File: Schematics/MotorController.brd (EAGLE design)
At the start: 90 x 80 mm, 47 parts, among them IC1 MEGA164P/324P/644P-AU, IC3 LM324N

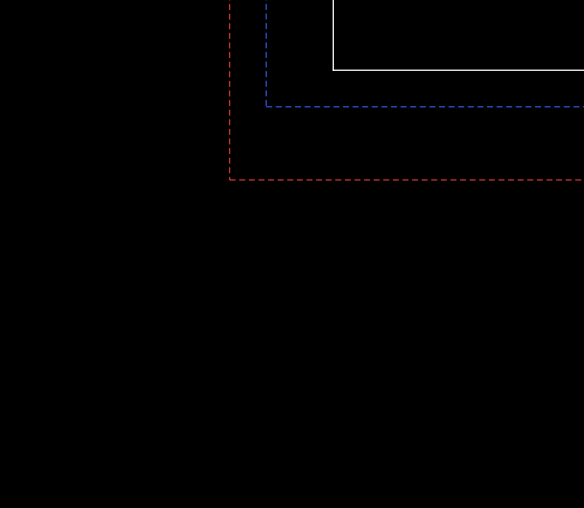
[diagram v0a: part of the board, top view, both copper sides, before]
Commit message: add files of device software newly created
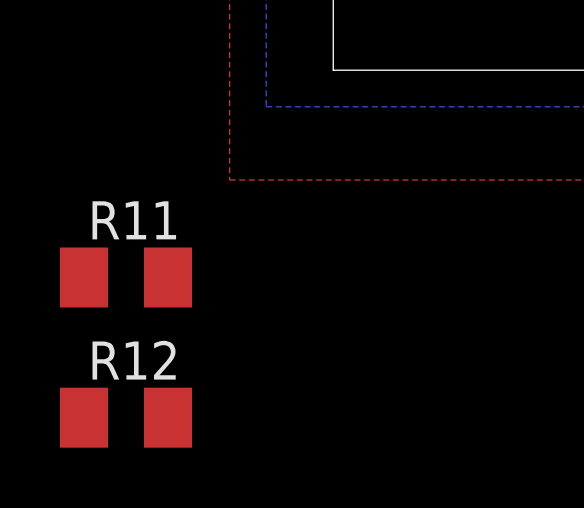
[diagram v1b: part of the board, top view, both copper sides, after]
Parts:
- added R11, R12: (no value), rcl:M3216
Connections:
- new net N$14: R10.2, R11.1, R12.1
- net +5V: no longer C11.2
- net A_BACK: now also R11.2; no longer R10.2
- net GND: now also C11.2, R12.2
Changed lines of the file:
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@@
 <element name="C14" library="rcl" package="C3216" value="" x="15.664" y="30.1504"/>
 <element name="L2" library="rcl" package="L3216C" value="" x="36" y="22" rot="R180"/>
+<element name="R11" library="rcl" package="M3216" value="" x="-6.9088" y="-6.9088"/>
+<element name="R12" library="rcl" package="M3216" value="" x="-6.9088" y="-11.5824"/>
 </elements>
 <signals>
@@
 <contactref element="C6" pad="2"/>
 <contactref element="C7" pad="2"/>
-<contactref element="C8" pad="1"/>
-<contactref element="C11" pad="2"/>
 <contactref element="U$3" pad="3"/>
 <contactref element="L2" pad="1"/>
-<wire x1="9.74" y1="48.26" x2="25.28" y2="50.18" width="0" layer="19" extent="1-1"/>
-<wire x1="6.6664" y1="53.7" x2="9.74" y2="48.26" width="0" layer="19" extent="1-1"/>
-<wire x1="10.0728" y1="34.504" x2="9.74" y2="48.26" width="0" layer="19" extent="1-1"/>
-<wire x1="4.29" y1="34.53" x2="10.0728" y2="34.504" width="0" layer="19" extent="1-1"/>
+<contactref element="C8" pad="1"/>
+<wire x1="6.6664" y1="53.7" x2="25.28" y2="50.18" width="0" layer="19" extent="1-1"/>
+<wire x1="4.29" y1="34.53" x2="6.6664" y2="53.7" width="0" layer="19" extent="1-1"/>
+<wire x1="10.0728" y1="34.504" x2="4.29" y2="34.53" width="0" layer="19" extent="1-1"/>
 <wire x1="6.896" y1="22.7052" x2="4.29" y2="34.53" width="0" layer="19" extent="1-1"/>
 <wire x1="12.934" y1="16.93" x2="6.896" y2="22.7052" width="0" layer="19" extent="1-1"/>
@@
 <vertex x="94.2848" y="84.1248"/>
 </polygon>
+<contactref element="C11" pad="2"/>
+<contactref element="R12" pad="2"/>
 <wire x1="30.45" y1="63.58" x2="36.16" y2="75.42" width="0" layer="19" extent="1-1"/>
 <wire x1="26.976" y1="62.58" x2="30.45" y2="63.58" width="0" layer="19" extent="1-1"/>
@@
 <wire x1="15.28" y1="53.68" x2="15.28" y2="56.18" width="0" layer="19" extent="1-1"/>
 <wire x1="15.28" y1="51.18" x2="15.28" y2="53.68" width="0" layer="19" extent="1-1"/>
-<wire x1="9.1796" y1="55.9536" x2="15.28" y2="56.18" width="0" layer="19" extent="1-1"/>
+<wire x1="9.22" y1="51.3328" x2="15.28" y2="51.18" width="0" layer="19" extent="1-1"/>
+<wire x1="9.74" y1="48.26" x2="9.22" y2="51.3328" width="0" layer="19" extent="1-1"/>
+<wire x1="9.1796" y1="55.9536" x2="9.22" y2="51.3328" width="0" layer="19" extent="1-1"/>
 <wire x1="6.6664" y1="55.4" x2="9.1796" y2="55.9536" width="0" layer="19" extent="1-1"/>
 <wire x1="6.74" y1="57.66" x2="6.6664" y2="55.4" width="0" layer="19" extent="1-1"/>
-<wire x1="9.22" y1="51.3328" x2="6.6664" y2="55.4" width="0" layer="19" extent="1-1"/>
-<wire x1="6.83" y1="42.15" x2="9.22" y2="51.3328" width="0" layer="19" extent="1-1"/>
+<wire x1="6.83" y1="42.15" x2="9.74" y2="48.26" width="0" layer="19" extent="1-1"/>
 <wire x1="9.8896" y1="38.3424" x2="6.83" y2="42.15" width="0" layer="19" extent="1-1"/>
 <wire x1="6.83" y1="31.99" x2="9.8896" y2="38.3424" width="0" layer="19" extent="1-1"/>
@@
 <wire x1="25.8064" y1="40.9956" x2="25.28" y2="51.18" width="0" layer="19" extent="1-1"/>
 <wire x1="4" y1="71.2" x2="15.6" y2="64.08" width="0" layer="19" extent="1-1"/>
+<wire x1="-5.5088" y1="-11.5824" x2="13.25" y2="8.26" width="0" layer="19" extent="1-1"/>
 </signal>
 <signal name="MISO">
@@
 <contactref element="D6" pad="E"/>
 <contactref element="D7" pad="E"/>
-<contactref element="R10" pad="2"/>
+<contactref element="R11" pad="2"/>
 <wire x1="3.7628" y1="62.8" x2="7.3564" y2="62.8" width="0" layer="19" extent="1-1"/>
-<wire x1="10.4992" y1="27.3056" x2="7.3564" y2="62.8" width="0" layer="19" extent="1-1"/>
+<wire x1="-5.5088" y1="-6.9088" x2="3.7628" y2="62.8" width="0" layer="19" extent="1-1"/>
 </signal>
 <signal name="N$6">
@@
 <wire x1="31.89553125" y1="18.826903125" x2="34.5" y2="22" width="0" layer="19" extent="1-1"/>
 </signal>
+<signal name="N$14">
+<contactref element="R10" pad="2"/>
+<contactref element="R12" pad="1"/>
+<contactref element="R11" pad="1"/>
+<wire x1="-8.3088" y1="-6.9088" x2="10.4992" y2="27.3056" width="0" layer="19" extent="1-1"/>
+<wire x1="-8.3088" y1="-11.5824" x2="-8.3088" y2="-6.9088" width="0" layer="19" extent="1-1"/>
+</signal>
 </signals>

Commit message: restoring
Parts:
- removed D5, D6, D7, D8: 1SS196, myparts:SC59-BEC
- removed L2: (no value), rcl:L3216C
- removed U$5: TLP621-2, myparts:SOCKET-08
- removed U$6, U$7: XH-2, myparts:XH-2
- added A, B, C, D: 942H, myparts:941H-2C-12D
- added A_NEXT, A_PREV, B_NEXT, B_PREV, C_NEXT, C_PREV, D_NEXT, D_PREV: XH-2, myparts:XH-2
- added C15, C18, C19, C24, C25: 0.1u, rcl:C0603
- added C16, C17: 0.47u, rcl:C0603
- added C20, C21: 22p, rcl:C0603
- added C22, C23: 4.7u, rcl:C0603
- added C26, C27: (no value), rcl:E2,5-6E
- added CONN: TUS_MODULE_SUPPLY, tus:2X08
- added F1, F2, F3, F4, F5: POLYSWITCH_20204/5, myparts:0204/5
- added IC2: MEGA164P/324P/644P-AU, avr-7:TQFP44
- added IC4: TLP621-2, myparts:SOCKET-08
- added LED3, LED5, LED7: G, led:LED3MM
- added LED4, LED6, LED8: O, led:LED3MM
- added R13, R14, R23, R24: 100, resistor:R0603
- added R15, R16, R22, R25: 25k, resistor:R0603
- added R17, R18, R20, R21, R30, R31: 3.3k, resistor:R0603
- added R19, R36, R37: 10k, resistor:R0603
- added R26, R27: 0.01, resistor:R1206
- added R28, R29: 33k, resistor:R0603
- added R32, R33: 500, resistor:R0603
- added R34, R35: 100k, resistor:R0603
- added T1, T2, T3, T4: 2SC1815, myparts:TO92-ECB
- C1, C2: device rcl:C1608 -> rcl:E2,5-6E
- C10: value (none) -> 0.47u; device rcl:E2-5 -> rcl:C0603
- C11, C7, C8: value (none) -> 0.1u; device rcl:C1608 -> rcl:C0603
- C12: value (none) -> 100u; device rcl:C1608 -> rcl:E2,5-6
- C13: value (none) -> 0.1u; device rcl:C3216 -> rcl:C0603
- C14: value (none) -> 100u; device rcl:C3216 -> rcl:E2-5
- C3: value (none) -> 0.1u; device rcl:E2-5 -> rcl:C0603
- C4: value (none) -> 0.1u; device rcl:E2,5-6 -> rcl:C0603
- C5, C6: value (none) -> 4.7u; device rcl:C1608 -> rcl:C0603
- C9: value (none) -> 0.47u; device rcl:C1608 -> rcl:C0603
- D1, D2, D3, D4: value 1SS196 -> 1N4148DO35-7; device myparts:SC59-BEC -> diode:DO35-7
- IC1: value MEGA164P/324P/644P-AU -> TLP621-2; device avr-7:TQFP44 -> myparts:SOCKET-08
- IC3: value LM324N -> OPA4234P; device linear:DIL14 -> burr-brown:DIL14
- JP1: value AVR-JTAG-10-R -> AVR-JTAG-10; device avr-7:AVR-JTAG-10R -> avr-7:AVR-JTAG-10
- L1: value (none) -> 47u
- LED1: value (none) -> G
- LED2: value (none) -> O
- Q1: value (none) -> 20.000M
- R1, R6: value (none) -> 100k; device rcl:M3216 -> resistor:R0603
- R10, R9: value (none) -> 33k; device rcl:M3216 -> resistor:R0603
- R11, R12: value (none) -> 0.01; device rcl:M3216 -> resistor:R1206
- R2, R4: value 100k -> 10k; device rcl:M3216 -> resistor:R0603
- R3: value 100k -> 500; device rcl:M3216 -> resistor:R0603
- R5: value (none) -> 500; device rcl:M3216 -> resistor:R0603
- R7, R8: value (none) -> 3.3k; device rcl:M3216 -> resistor:R0603
- U$1: value 942H -> TB6559; device myparts:942H -> myparts:HSOP-16
- U$2: value TUS_MODULE_SUPPLY -> TB6559; device tus:2X08 -> myparts:HSOP-16
- U$4: value POLYSWITCH_20207/10 -> TB6559; device myparts:0207/10 -> myparts:HSOP-16
- moved R11 100.5 mm to (73.8, 53.0)
- moved C3 79.0 mm to (78.6, 62.3)
- moved C5 76.8 mm to (78.6, 59.3), turned to 180 degrees
- moved R12 73.1 mm to (28.9, 52.2)
- moved C1 71.1 mm to (54.1, 65.8)
- moved D4 70.0 mm to (59.7, 6.30)
- moved C13 64.9 mm to (76.2, 38.8), turned to 0 degrees
- moved R9 62.9 mm to (73.6, 56.3), turned to 0 degrees
- moved IC1 60.4 mm to (44.5, 72.3), turned to 180 degrees
- moved C2 58.0 mm to (28.4, 65.0)
- moved D3 54.2 mm to (30.7, 6.30)
- moved C6 50.8 mm to (34.5, 58.9)
- moved IC3 50.0 mm to (75.8, 39.0), turned to 180 degrees
- moved U$4 49.7 mm to (70.9, 21.3)
- moved C7 49.4 mm to (55.7, 56.2), turned to 270 degrees
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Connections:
- removed net A_BACK: D6.E, D7.E, R11.2
- removed net A_CONN1: U$1.2, U$6.P$1
- removed net A_CONN2: U$1.'2, U$6.P$2
- removed net A_NEXT1: U$1.3, U$7.P$1
- removed net A_NEXT2: U$1.'3, U$7.P$2
- removed net CTRL_A_FEEDBACK: C14.2, IC1.37, IC3.1, IC3.2
- removed net CTRL_B_FEEDBACK: IC1.36
- removed net CTRL_C_FEEDBACK: IC1.35
- removed net CTRL_D_FEEDBACK: IC1.34
- removed net CTRL_PWM: D4.E, U$3.14
- new net A_OUT3: C.8, R20.2, U$3.7
- new net A_OUT4: C.9, LED5.A, LED6.K, U$3.9
- new net A_OUT5: B.8, R18.2, U$2.7
- new net A_OUT6: B.9, LED1.A, LED2.K, U$2.9
- new net A_OUT7: D.8, R21.2, U$4.7
- new net A_OUT8: D.9, LED7.A, LED8.K, U$4.9
- new net D: D.4, D_PREV.P$2
- new net FEEDBACK_A: IC2.35, IC3.1, R16.2
- new net FEEDBACK_B: IC2.34, IC3.7, R15.2
- new net FEEDBACK_C: IC2.36, IC3.14, R25.2
- new net FEEDBACK_D: IC2.37, IC3.8, R22.2
- new net N$15: A.11, A_NEXT.P$1
- new net N$16: A.4, A_PREV.P$2
- new net N$17: A.13, A_PREV.P$1
- new net N$18: C18.2, C27.+, F4.1, U$3.5
- new net N$19: LED5.K, LED6.A, R20.1
- new net N$20: IC1.3, R5.2
- new net N$21: C9.1, IC3.3, R9.2
- new net N$22: C.6, C_NEXT.P$2
- new net N$23: C.11, C_NEXT.P$1
- new net N$24: C.4, C_PREV.P$2
- new net N$25: C.13, C_PREV.P$1
- new net N$26: IC4.5, R35.1, R36.1
- new net N$27: C.16, D3.C, T3.E
- new net N$28: R36.2, T3.B
- new net N$29: IC3.13, R24.1, R25.1
- new net N$30: C16.1, IC3.12, R28.2
- new net N$31: R26.1, R28.1, U$3.10
- new net N$32: C4.1, U$2.15
- new net N$33: R8.1, U$2.11
- new net N$34: C2.+, C8.2, F1.1, U$2.5
- new net N$35: LED1.K, LED2.A, R18.1
- new net N$36: IC4.1, R33.2
- new net N$37: B.6, B_NEXT.P$2
- new net N$38: B.11, B_NEXT.P$1
- new net N$39: B.4, B_PREV.P$2
- new net N$40: B.13, B_PREV.P$1
- new net N$41: IC1.5, R1.1, R4.1
- new net N$42: B.16, D2.C, T1.E
- new net N$43: R4.2, T1.B
- new net N$44: IC3.6, R13.1, R15.1
- new net N$45: C10.1, IC3.5, R10.2
- new net N$46: R10.1, R12.1, U$2.10
- new net N$47: C25.1, U$4.15
- new net N$48: R31.1, U$4.11
- new net N$49: C19.2, C26.+, F5.1, U$4.5
- new net N$50: LED7.K, LED8.A, R21.1
- new net N$51: IC4.3, R32.2
- new net N$52: D.6, D_NEXT.P$2
- new net N$53: D.11, D_NEXT.P$1
- new net N$54: CONN.6, F3.1
- new net N$55: D.13, D_PREV.P$1
- new net N$56: IC4.7, R34.1, R37.1
- new net N$57: D.16, D4.C, T4.E
- new net N$58: R37.2, T4.B
- new net N$59: IC3.9, R22.1, R23.1
- new net N$60: C17.1, IC3.10, R29.2
- new net N$61: R27.1, R29.1, U$4.10
- new net N$84: A.16, D1.C, T2.E
- new net N$86: R2.2, T2.B
- net !RESET: now also CONN.15, IC2.4, JP1.6, R19.2; no longer IC1.4, R1.2, U$2.15
- net !SS: now also CONN.11, IC2.44; no longer IC1.44, U$2.11
- net +12V: now also C12.+, CONN.1, CONN.2, CONN.4, F1.2, F2.2, F4.2, F5.2, IC1.6, IC1.8, IC4.6, IC4.8, T1.C, T2.C, T3.C, T4.C; no longer C10.+, C4.+, C9.2, D8.E, IC3.4, R8.1, U$2.1, U$2.2, U$2.4, U$4.2
- net +5V: now also C11.2, C13.2, C14.+, C15.2, F3.2, IC2.17, IC2.38, IC2.5, IC3.4, R19.1, U$1.3, U$2.3, U$4.3; no longer C3.+, C5.2, C6.2, C7.2, C8.1, IC1.17, IC1.38, IC1.5, L2.1, R1.1, U$2.6
- net A_OUT1: now also A.8, R17.2, U$1.7; no longer D6.C, R6.2, U$1.1, U$3.7
- net A_OUT2: now also A.9, LED3.A, LED4.K, U$1.9; no longer D7.C, LED1.K, LED2.A, U$1.'1, U$3.9
- net CTRL_A_1: now also IC2.32, U$1.1; no longer D3.E, IC1.9, R2.2, U$3.1
- net CTRL_A_2: now also IC2.31, U$1.16; no longer D1.E, IC1.10, R3.2, U$3.16
- net CTRL_A_3: now also IC2.33, R3.1, U$1.2; no longer D2.E, IC1.11, R4.2, R7.1, U$3.2
- net CTRL_A_ALERT: now also C5.1, IC2.30, R7.2; no longer C12.1, D5.E, IC1.12, R5.2
- net CTRL_A_PWM: now also IC2.15, U$1.14; no longer IC1.14
- net CTRL_B_1: now also IC2.42, U$2.1; no longer IC1.19
- net CTRL_B_2: now also IC2.41, U$2.16; no longer IC1.20
- net CTRL_B_3: now also IC2.43, R5.1, U$2.2; no longer IC1.25
- net CTRL_B_ALERT: now also C6.1, IC2.40, R8.2; no longer IC1.26
- net CTRL_B_PWM: now also IC2.13, U$2.14; no longer IC1.13
- net CTRL_C_1: now also IC2.11, U$3.1; no longer IC1.40
- net CTRL_C_2: now also IC2.10, U$3.16; no longer IC1.41
- net CTRL_C_3: now also IC2.12, R32.1, U$3.2; no longer IC1.42
- net CTRL_C_ALERT: now also C22.1, IC2.9, R30.2; no longer IC1.43
- net CTRL_C_PWM: now also IC2.16, U$3.14; no longer IC1.16
- net CTRL_D_1: now also IC2.26, U$4.1; no longer IC1.33
- net CTRL_D_2: now also IC2.25, U$4.16; no longer IC1.32
- net CTRL_D_3: now also IC2.19, R33.1, U$4.2; no longer IC1.31
- net CTRL_D_ALERT: now also C23.1, IC2.20, R31.2; no longer IC1.30
- net CTRL_D_PWM: now also IC2.14, U$4.14; no longer IC1.15
- net GND: now also A.1, B.1, C.1, C1.-, C10.2, C11.1, C12.-, C13.1, C14.-, C15.1, C16.2, C17.2, C18.1, C19.1, C2.-, C20.1, C21.1, C22.2, C23.2, C24.2, C25.2, C26.-, C27.-, C3.2, C4.2, C5.2, C6.2, C8.1, C9.2, CONN.12, CONN.3, CONN.5, CONN.7, CONN.8, CONN.9, D.1, D1.A, D2.A, D3.A, D4.A, IC1.2, IC1.4, IC2.18, IC2.28, IC2.39, IC2.6, IC4.2, IC4.4, R1.2, R11.2, R13.2, R14.2, R23.2, R24.2, R26.2, R27.2, R34.2, R35.2, R6.2, U$1.12, U$1.13, U$1.8, U$1.FIN_1, U$1.FIN_2, U$2.13, U$2.4, U$2.FIN_1, U$2.FIN_2, U$4.12, U$4.13, U$4.4, U$4.8, U$4.FIN_1, U$4.FIN_2; no longer C1.1, C10.-, C11.2, C12.2, C13.2, C2.1, C3.-, C4.-, C5.1, C6.1, C8.2, C9.1, D1.C, D2.C, D3.C, D4.C, D5.C, D8.C, IC1.18, IC1.28, IC1.39, IC1.6, R2.1, R3.1, R4.1, U$2.3, U$2.5, U$2.7, U$2.9, U$3.10, U$5.2
- net MISO: now also CONN.14, IC2.2; no longer IC1.2, U$2.14
- net MOSI: now also CONN.16, IC2.1; no longer IC1.1, U$2.16
- net N$1: now also IC2.27, IC2.29; no longer IC1.27
- net N$10: now also C1.+, C7.2, F2.1, U$1.5; no longer U$3.5, U$4.1
- net N$11: now also IC3.2, R14.1, R16.1; no longer C14.1, R10.1, R9.2
- net N$12: now also R30.1, U$3.11; no longer C13.1, IC3.3, R9.1
- net N$13: now also A.6, A_NEXT.P$2; no longer IC1.29, L2.2
- net N$14: now also R9.1, U$1.10; no longer R10.2, R12.1
- net N$2: now also C21.2, IC2.7; no longer C1.2, IC1.7
- net N$3: now also C20.2, IC2.8; no longer C2.2, IC1.8
- net N$4: now also R7.1, U$1.11; no longer R5.1, U$3.11
- net N$5: now also C3.1, U$1.15; no longer C11.1, U$3.15
- net N$6: now also IC1.1, R3.2; no longer R7.2, U$5.1
- net N$7: now also IC1.7, R2.1, R6.1; no longer U$1.'4, U$5.7
- net N$8: now also LED3.K, LED4.A, R17.1; no longer LED1.A, LED2.K, R6.1
- net N$9: now also C24.1, U$3.15; no longer R8.2, U$5.8
- net SCK: now also CONN.13, IC2.3; no longer IC1.3, U$2.13
- net TCK: now also IC2.21; no longer IC1.21
- net TDI: now also IC2.24; no longer IC1.24
- net TDO: now also IC2.23; no longer IC1.23
- net TMS: now also IC2.22; no longer IC1.22
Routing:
- net +12V: track 0.00 -> 217.0 mm
- net +5V: track 0.00 -> 203.8 mm, vias 0 -> 12
- net N$30: track 0.00 -> 96.6 mm, vias 0 -> 3
- net TDO: track 0.00 -> 84.3 mm, vias 0 -> 7
- net CTRL_B_3: track 0.00 -> 71.4 mm, vias 0 -> 5
- net !RESET: track 0.00 -> 68.6 mm, vias 0 -> 3
- net A_OUT6: track 0.00 -> 60.4 mm
- net CTRL_D_3: track 0.00 -> 57.2 mm
- net N$45: track 0.00 -> 57.0 mm, vias 0 -> 3
- net FEEDBACK_C: track 0.00 -> 56.5 mm, vias 0 -> 1
- net A_OUT3: track 0.00 -> 55.8 mm, vias 0 -> 2
- net TDI: track 0.00 -> 55.6 mm, vias 0 -> 7
- net A_OUT1: track 0.00 -> 55.5 mm, vias 0 -> 2
- net FEEDBACK_A: track 0.00 -> 54.7 mm, vias 0 -> 1
- net A_OUT8: track 0.00 -> 54.6 mm, vias 0 -> 2
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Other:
- board text added: "D48245"
- board text added: "T.U.S. module_MotorControl"
- board text added: "https://github.com/sosoru/TrainUtilizingSystem"
- board text added: "module_MotorControl"
